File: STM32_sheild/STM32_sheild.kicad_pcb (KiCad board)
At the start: 2 copper layers, 70 x 57.5 mm, 48 parts, among them J1 61612002121503, J2 CN7, J3 CN10, J4 632722100213, J5 691210910002, J6 691210910002, U1 OPA333xxDBV, U2 TPS63031DSK, U3 MCP73831-2-MC, U4 OPA333xxDBV

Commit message: Changes to layout
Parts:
- moved C6 75.7 mm to (148.0, 81.5)
- moved C7 75.7 mm to (153.2, 81.5)
- moved J4 72.4 mm to (172.8, 122.8), turned to 90 degrees
- moved C5 67.1 mm to (148.5, 100.0)
- moved C8 67.1 mm to (144.0, 95.5)
- moved R9 58.1 mm to (165.3, 118.2), turned to -90 degrees
- moved R8 58.0 mm to (165.3, 127.3), turned to 90 degrees
- moved J6 47.4 mm to (151.5, 71.5)
- moved L1 42.0 mm to (147.5, 87.5), turned to -90 degrees
- moved C4 39.8 mm to (159.0, 116.0)
- moved C9 33.5 mm to (151.8, 115.8), turned to -90 degrees
- moved U3 32.6 mm to (152.9, 121.7), turned to 180 degrees
- moved U2 27.1 mm to (152.2, 87.4)
- moved R10 24.4 mm to (148.8, 123.3), turned to 90 degrees
- moved JP2 22.8 mm to (129.0, 72.5), turned to 90 degrees
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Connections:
- C10 pad 1: /OPA_VDD -> /OPA2_VDD
- C11 pad 1: /OPA_VDD -> /OPA2_VDD
- D4 pad 1: /OPA_IN+ -> GND
- D4 pad 2: GND -> /OPA2_IN+
- R11 pad 2: /OPA_IN+ -> /OPA2_IN+
- R12 pad 1: /OPA_IN- -> /OPA2_IN-
- R13 pad 1: /OPA_IN- -> /OPA2_IN-
- R13 pad 2: /OPA_out -> /OPA2_out
- R14 pad 1: /OPA_out -> /OPA2_out
- R15 pad 1: /OPA_VDD -> /OPA2_VDD
- U4 pad 1: /OPA_out -> /OPA2_out
- U4 pad 3: /OPA_IN+ -> /OPA2_IN+
- U4 pad 4: /OPA_IN- -> /OPA2_IN-
- U4 pad 5: /OPA_VDD -> /OPA2_VDD
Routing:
- net /OPA2_out: track 0.00 -> 33.3 mm
- net Net-(JP2-C): track 0.00 -> 14.3 mm
- net /OPA2_VDD: track 0.00 -> 12.7 mm
- net /ADC2: track 0.00 -> 9.42 mm
- net Net-(J5-Pad1): track 0.00 -> 9.09 mm
- net /OPA2_IN-: track 0.00 -> 6.92 mm
- net /OPA2_IN+: track 0.00 -> 6.25 mm
- net Net-(U2-L1): track 0.00 -> 3.86 mm
- net Net-(U2-L2): track 0.00 -> 3.78 mm

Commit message: changes to layout
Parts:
- moved C8 18.8 mm to (160.0, 85.5)
- moved R7 10.7 mm to (160.5, 90.6), turned to 90 degrees
- moved C5 10.1 mm to (152.0, 90.5), turned to 0 degrees
- moved D3 7.95 mm to (160.5, 95.0), turned to 90 degrees
- moved C6 4.00 mm to (152.0, 81.5), turned to 0 degrees
- moved B1 3.17 mm to (139.0, 142.5)
- moved C7 2.78 mm to (152.0, 84.0), turned to 0 degrees
- moved L1 0.50 mm to (148.0, 87.5)
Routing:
- net +BATT: track 0.50 -> 1.09 mm
- net Net-(U2-L2): track 3.78 -> 3.28 mm
- net Net-(U2-L1): track 3.86 -> 3.36 mm
- added copper zone on F.Cu, net +BATT
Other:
- board size 70 x 57.5 mm -> 70 x 67 mm

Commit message: Added mulitple pours in layout
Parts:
- moved R8 30.5 mm to (149.0, 101.5)
- moved R6 26.9 mm to (148.0, 95.0)
- moved D2 26.4 mm to (144.0, 95.0)
- moved R9 25.6 mm to (146.0, 101.5), turned to 90 degrees
- moved R10 25.3 mm to (148.0, 98.0), turned to 180 degrees
- moved U3 24.0 mm to (152.6, 97.7)
- moved J4 23.1 mm to (156.5, 106.5), turned to 0 degrees
- moved C9 21.4 mm to (156.5, 95.0), turned to 0 degrees
- moved B1 19.1 mm to (128.5, 126.5)
- moved C4 18.0 mm to (158.0, 98.0), turned to 0 degrees
- moved D3 16.0 mm to (160.0, 79.0)
- moved R7 7.10 mm to (160.0, 83.5)
- moved C8 3.81 mm to (156.5, 87.0)
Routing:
- net +BATT: track 1.09 -> 59.7 mm
- net +3.3V_REG: track 0.00 -> 28.1 mm
- net V_USB: track 0.35 -> 15.6 mm
- net Net-(U2-EN): track 0.00 -> 4.09 mm
- net Net-(U3-STAT): track 0.00 -> 3.53 mm
- net Net-(J4-CC2): track 12.6 -> 15.9 mm
- net Net-(D3-K): track 0.00 -> 2.65 mm
- net Net-(U3-PROG): track 0.00 -> 2.38 mm
- net Net-(D2-K): track 0.00 -> 2.15 mm
- net Net-(J4-CC1): track 13.1 -> 11.2 mm
- net /OPA2_out: track 33.3 -> 31.9 mm
- added copper zone on B.Cu, net GND
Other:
- board size 70 x 67 mm -> 87 x 83.5 mm

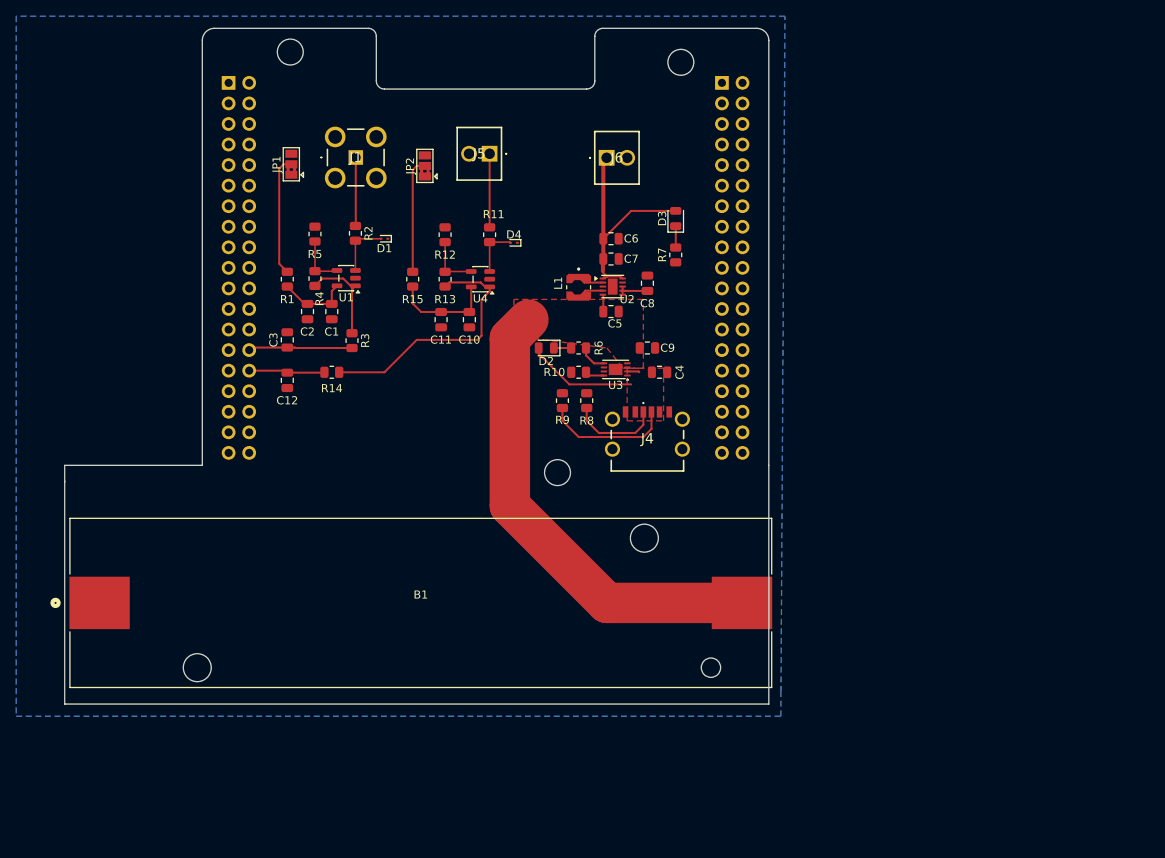
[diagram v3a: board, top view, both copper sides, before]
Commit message: Added ground plane
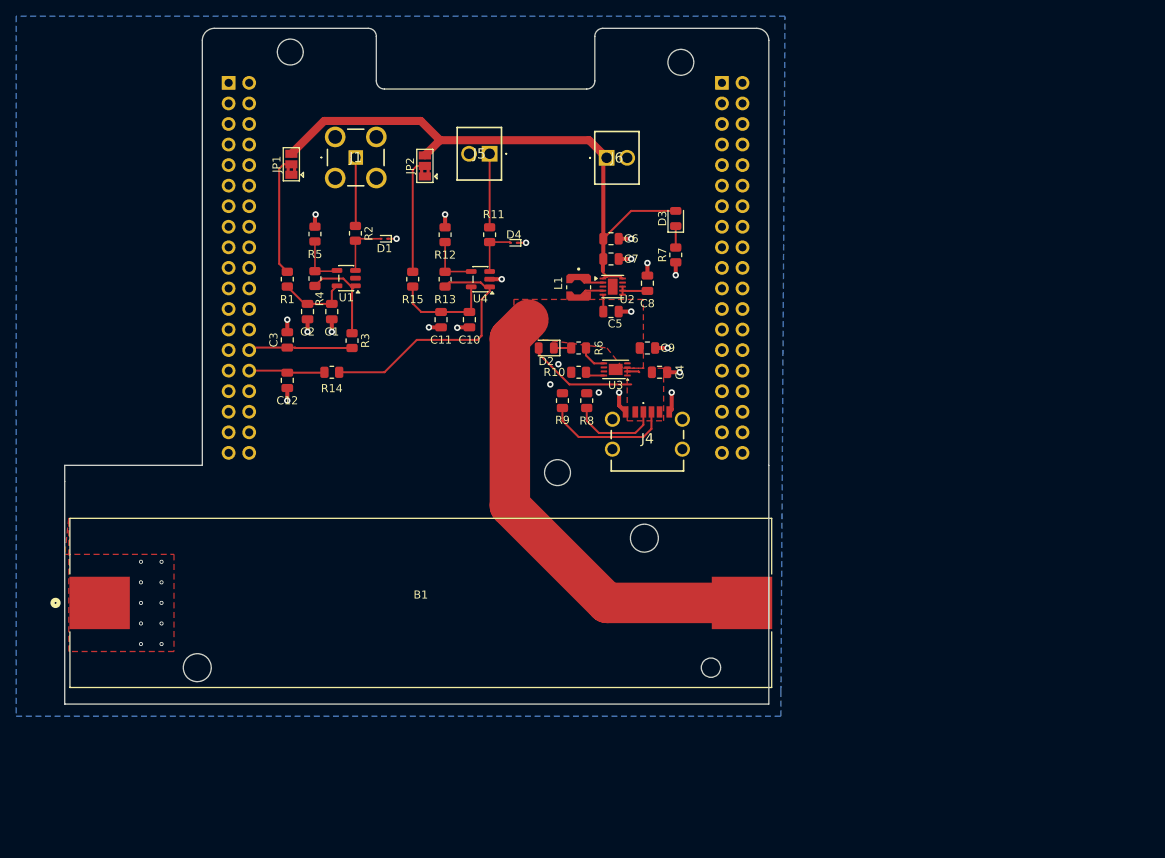
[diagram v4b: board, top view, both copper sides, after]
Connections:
- JP1 pad 3: +3.3V -> +3.3V_REG
- JP2 pad 3: +3.3V -> +3.3V_REG
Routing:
- net +3.3V_REG: track 28.1 -> 73.2 mm
- net GND: track 0.00 -> 32.2 mm, vias 0 -> 33
- added copper zone on F.Cu, net GND

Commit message: random updates
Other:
- board text added: "Nitrox analyzer Prototype board"
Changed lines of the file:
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@@
 		(tags "resistor")
 		(property "Reference" "R5"
-			(at -2.5 0 180)
+			(at 2.42 1.08 180)
 			(layer "F.SilkS")
 			(effects
@@
 		(tags "WSON NoLead")
 		(property "Reference" "U2"
-			(at 1.7875 1.5875 0)
+			(at 1.2875 -1.9125 0)
 			(layer "F.SilkS")
 			(effects
@@
 		(tags "resistor")
 		(property "Reference" "R2"
-			(at 0 -1.65 90)
+			(at -2.3325 -0.08 180)
 			(layer "F.SilkS")
 			(effects
@@
 		(tags "capacitor")
 		(property "Reference" "C9"
-			(at 2.5 0 180)
+			(at 2.5 1 180)
 			(layer "F.SilkS")
 			(effects
@@
 		)
 		(property "Value" "4.7uF"
-			(at 2 -2 0)
+			(at 0.5 -1.5 0)
 			(layer "F.Fab")
 			(effects
@@
 		(at 148 87.5 -90)
 		(property "Reference" "L1"
-			(at -0.5 2.5 90)
+			(at 0 2.5 270)
 			(layer "F.SilkS")
 			(effects
@@
 		(tags "SOT TO_SOT_SMD")
 		(property "Reference" "U1"
-			(at 0 -2.4 0)
+			(at -0.2175 2.37 0)
 			(layer "F.SilkS")
 			(effects
@@
 		(tags "resistor")
 		(property "Reference" "R12"
-			(at -2.5 0 180)
+			(at 2.5 1.5 180)
 			(layer "F.SilkS")
 			(effects
@@
 		(tags "SOT TO_SOT_SMD")
 		(property "Reference" "U4"
-			(at 0 -2.4 0)
+			(at -0.6375 2.5 0)
 			(layer "F.SilkS")
 			(effects
@@
 		)
 		(property "Value" "OPA333xxDBV"
-			(at -3.1375 2.4 0)
+			(at -4.1375 -2.5 0)
 			(layer "F.Fab")
 			(effects
@@
 		(tags "capacitor")
 		(property "Reference" "C7"
-			(at 2.5 0 0)
+			(at 2.5 -0.5 0)
 			(layer "F.SilkS")
 			(effects
@@
 		)
 		(property "Value" "2.2k"
-			(at -4 0 0)
+			(at -3.5 -1 0)
 			(layer "F.Fab")
 			(effects
@@
 		(tags "capacitor")
 		(property "Reference" "C2"
-			(at 2.5 0 180)
+			(at 2.5 0.5 270)
 			(layer "F.SilkS")
 			(effects
@@
 		)
 		(property "Value" "10uF"
-			(at 0 1.68 90)
+			(at 0.5 1.5 90)
 			(layer "F.Fab")
 			(effects
@@
 		(tags "capacitor")
 		(property "Reference" "C4"
-			(at 2.5 0 90)
+			(at 2.5 1 180)
 			(layer "F.SilkS")
 			(effects
@@
 		(tags "resistor")
 		(property "Reference" "R4"
-			(at 2.5 -0.58 90)
+			(at 2.08 -0.58 180)
 			(layer "F.SilkS")
 			(effects
@@
 		(tags "resistor")
 		(property "Reference" "R11"
-			(at -2.5 -0.5 180)
+			(at -2.5 -1 180)
 			(layer "F.SilkS")
 			(effects
@@
 		(tags "capacitor")
 		(property "Reference" "C12"
-			(at 2.5 0 180)
+			(at 1 1.5 270)
 			(layer "F.SilkS")
 			(effects
@@
 		)
 		(property "Value" "10uF"
-			(at 0 -2.5 90)
+			(at 1 -2 90)
 			(layer "F.Fab")
 			(effects
@@
 		(tags "capacitor")
 		(property "Reference" "C6"
-			(at 2.5 0 180)
+			(at 2.5 -1 180)
 			(layer "F.SilkS")
 			(effects
@@
 		(tags "capacitor")
 		(property "Reference" "C1"
-			(at 2.5 0 180)
+			(at 2.5 0.5 270)
 			(layer "F.SilkS")
 			(effects
@@
 		)
 		(property "Value" "100n"
-			(at 0 -1.5 90)
+			(at 0.5 1.5 90)
 			(layer "F.Fab")
 			(effects
@@
 		)
 	)
+	(gr_rect
+		(start 109.5 64.5)
+		(end 126.5 102.5)
+		(stroke
+			(width 0.15)
+			(type default)
+		)
+		(fill no)
+		(layer "F.SilkS")
+	)
+	(gr_rect
+		(start 126.5 64.5)
+		(end 142 102.5)
+		(stroke
+			(width 0.15)
+			(type default)
+		)
+		(fill no)
+		(layer "F.SilkS")
+	)
+	(gr_rect
+		(start 142 64.5)
+		(end 162.5 92.5)
+		(stroke
+			(width 0.15)
+			(type default)
+		)
+		(fill no)
+		(layer "F.SilkS")
+	)
+	(gr_rect
+		(start 142 92.5)
+		(end 162.5 114)
+		(stroke
+			(width 0.15)
+			(type default)
+		)
+		(fill no)
+		(layer "F.SilkS")
+	)
 	(gr_line
 		(start 84.5 109.5)
@@
 		(layer "Edge.Cuts")
 	)
+	(gr_text "Nitrox analyzer\nPrototype board"
+		(at 113.5 109 0)
+		(layer "F.SilkS")
+		(effects
+			(font
+				(size 1.5 1.5)
+				(thickness 0.3)
+				(bold yes)
+			)
+			(justify left bottom)
+		)
+	)
 	(segment
 		(start 149.3125 98.4)
@@
 	)
 	(segment
-		(start 151 86.9125)
-		(end 148.6825 86.9125)
+		(start 148 86.23)
+		(end 148.77 87)
+		(width 0.5)
+		(layer "F.Cu")
+		(net "Net-(U2-L2)")
+	)
+	(segment
+		(start 148.77 87)
+		(end 150 87)
+		(width 0.5)
+		(layer "F.Cu")
+		(net "Net-(U2-L2)")
+	)
+	(segment
+		(start 150.0875 86.9125)
+		(end 151 86.9125)
 		(width 0.25)
 		(layer "F.Cu")
@@
 	)
 	(segment
-		(start 148.6825 86.9125)
-		(end 148 86.23)
+		(start 150 87)
+		(end 150.0875 86.9125)
 		(width 0.25)
 		(layer "F.Cu")
@@
 	)
 	(segment
-		(start 148.8575 87.9125)
-		(end 148 88.77)
+		(start 148.77 88)
+		(end 150 88)
+		(width 0.5)
+		(layer "F.Cu")
+		(net "Net-(U2-L1)")
+	)
+	(segment
+		(start 150.110666 87.9125)
+		(end 151 87.9125)
+		(width 0.25)
+		(layer "F.Cu")
+		(net "Net-(U2-L1)")
+	)
+	(segment
+		(start 148 88.77)
+		(end 148.77 88)
+		(width 0.5)
+		(layer "F.Cu")
+		(net "Net-(U2-L1)")
+	)
+	(segment
+		(start 150 88)
+		(end 150.023166 88)
 		(width 0.25)
 		(layer "F.Cu")
@@
 	)
 	(segment
-		(start 151 87.9125)
-		(end 148.8575 87.9125)
+		(start 150.023166 88)
+		(end 150.110666 87.9125)
 		(width 0.25)
 		(layer "F.Cu")

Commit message: update
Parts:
- removed J4: 632722100213, KiCad_wurth_USB-C_PD_connector:632722100213
- added J7: 629722010114, Connector_SMD_Wurth:J_Wurth_WR-USB_629722010114, F.Cu at (156.6, 103.8)
- moved R9 5.41 mm to (149.0, 106.0), turned to -90 degrees
- moved R8 0.50 mm to (149.0, 102.0)
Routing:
- net Net-(J7-CC2): track 15.9 -> 7.93 mm
- net GND: track 32.2 -> 38.5 mm
- net V_USB: track 15.6 -> 20.8 mm
- net Net-(J7-CC1): track 11.2 -> 7.80 mm

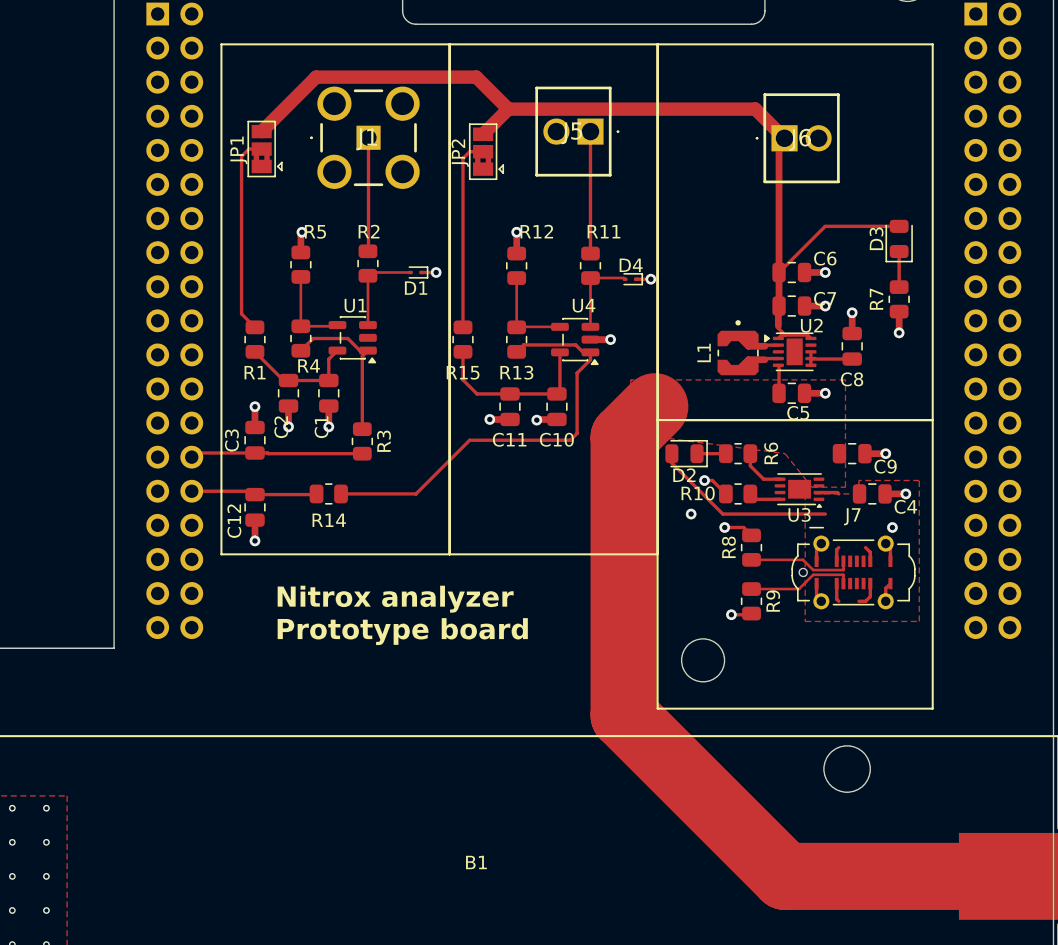
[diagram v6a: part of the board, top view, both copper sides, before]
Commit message: added I2C pins
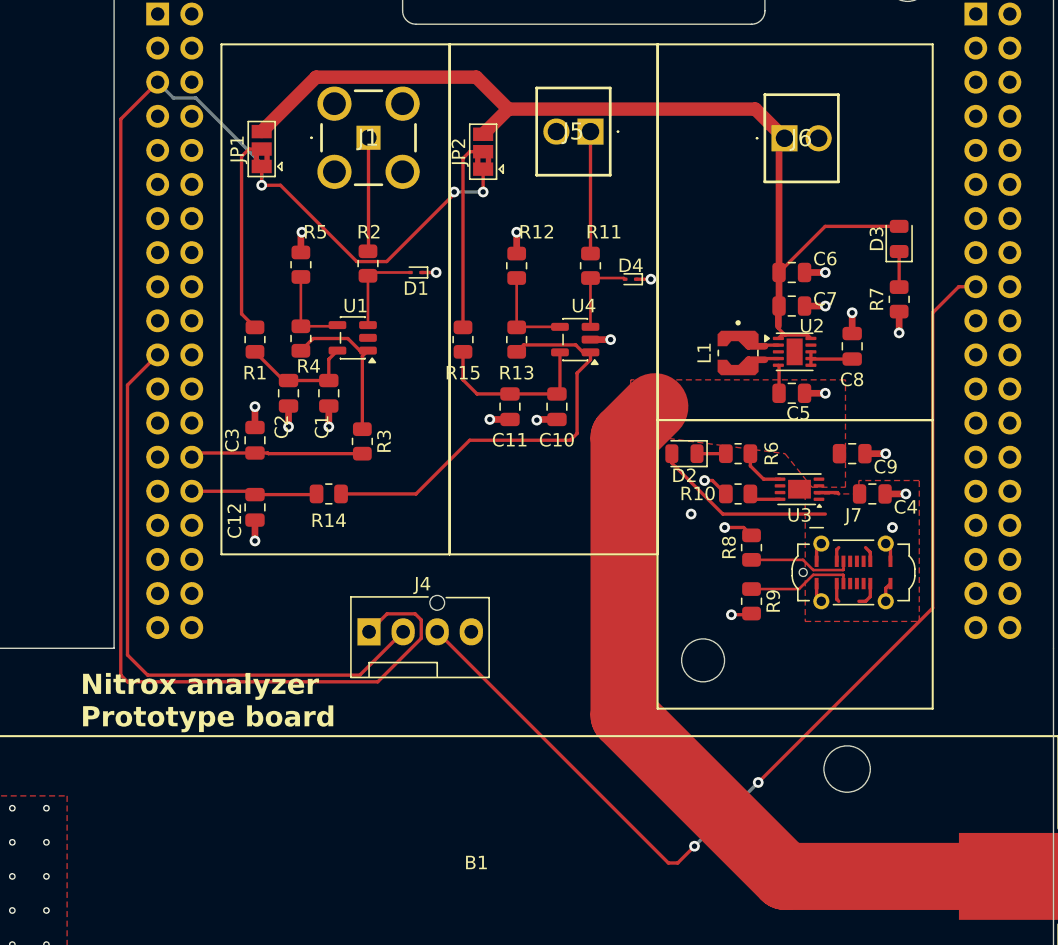
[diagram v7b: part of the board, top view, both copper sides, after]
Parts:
- added J4: Conn_01x04_Pin, Connector:FanPinHeader_1x04_P2.54mm_Vertical, F.Cu at (120.5, 108.3)
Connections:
- J2 pad 21: unconnected-(J2-Pin_21-Pad21) -> /SDA
- J3 pad 17: unconnected-(J3-Pin_17-Pad17) -> /SCL
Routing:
- net VDD: track 0.00 -> 111.3 mm, vias 0 -> 3
- net /SCL: track 0.00 -> 77.9 mm, vias 0 -> 2
- net /SDA: track 0.00 -> 45.8 mm
